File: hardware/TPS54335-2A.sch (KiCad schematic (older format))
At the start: 17 parts, among them J1 header, U1 TPS54335-2A

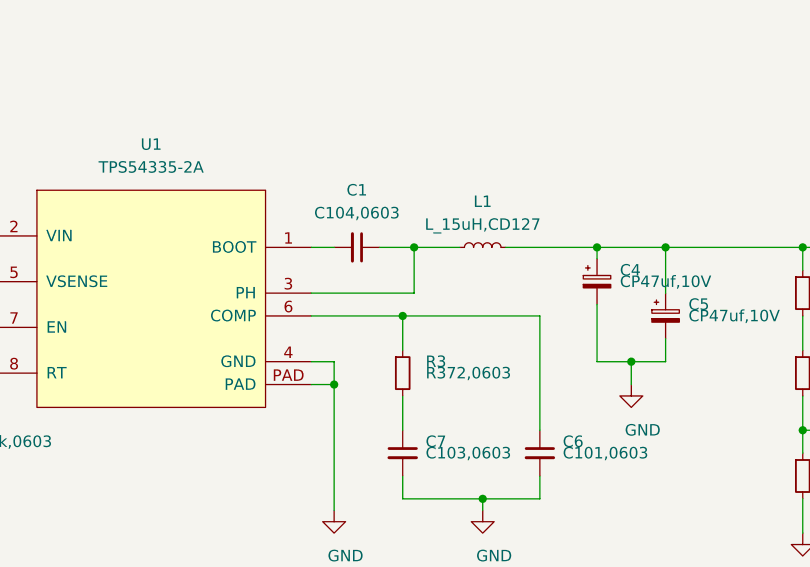
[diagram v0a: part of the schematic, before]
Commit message: update for track width,
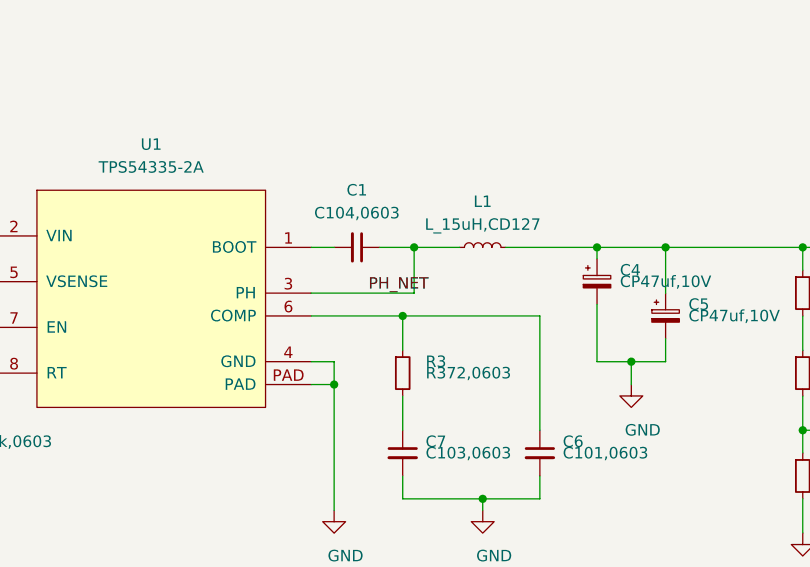
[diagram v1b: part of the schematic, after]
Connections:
- net PH_NET: now reaches C1.1, L1.1, U1.3 (PH)
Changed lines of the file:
@@
 EESchema Schematic File Version 4
+LIBS:TPS54335-2A-cache
 EELAYER 29 0
 EELAYER END
@@
 EndData
 $EndBitmap
+Text Label 5050 2000 0    50   ~ 0
+PH_NET
 $EndSCHEMATC
